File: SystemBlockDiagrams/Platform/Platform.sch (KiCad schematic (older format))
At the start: 21 parts

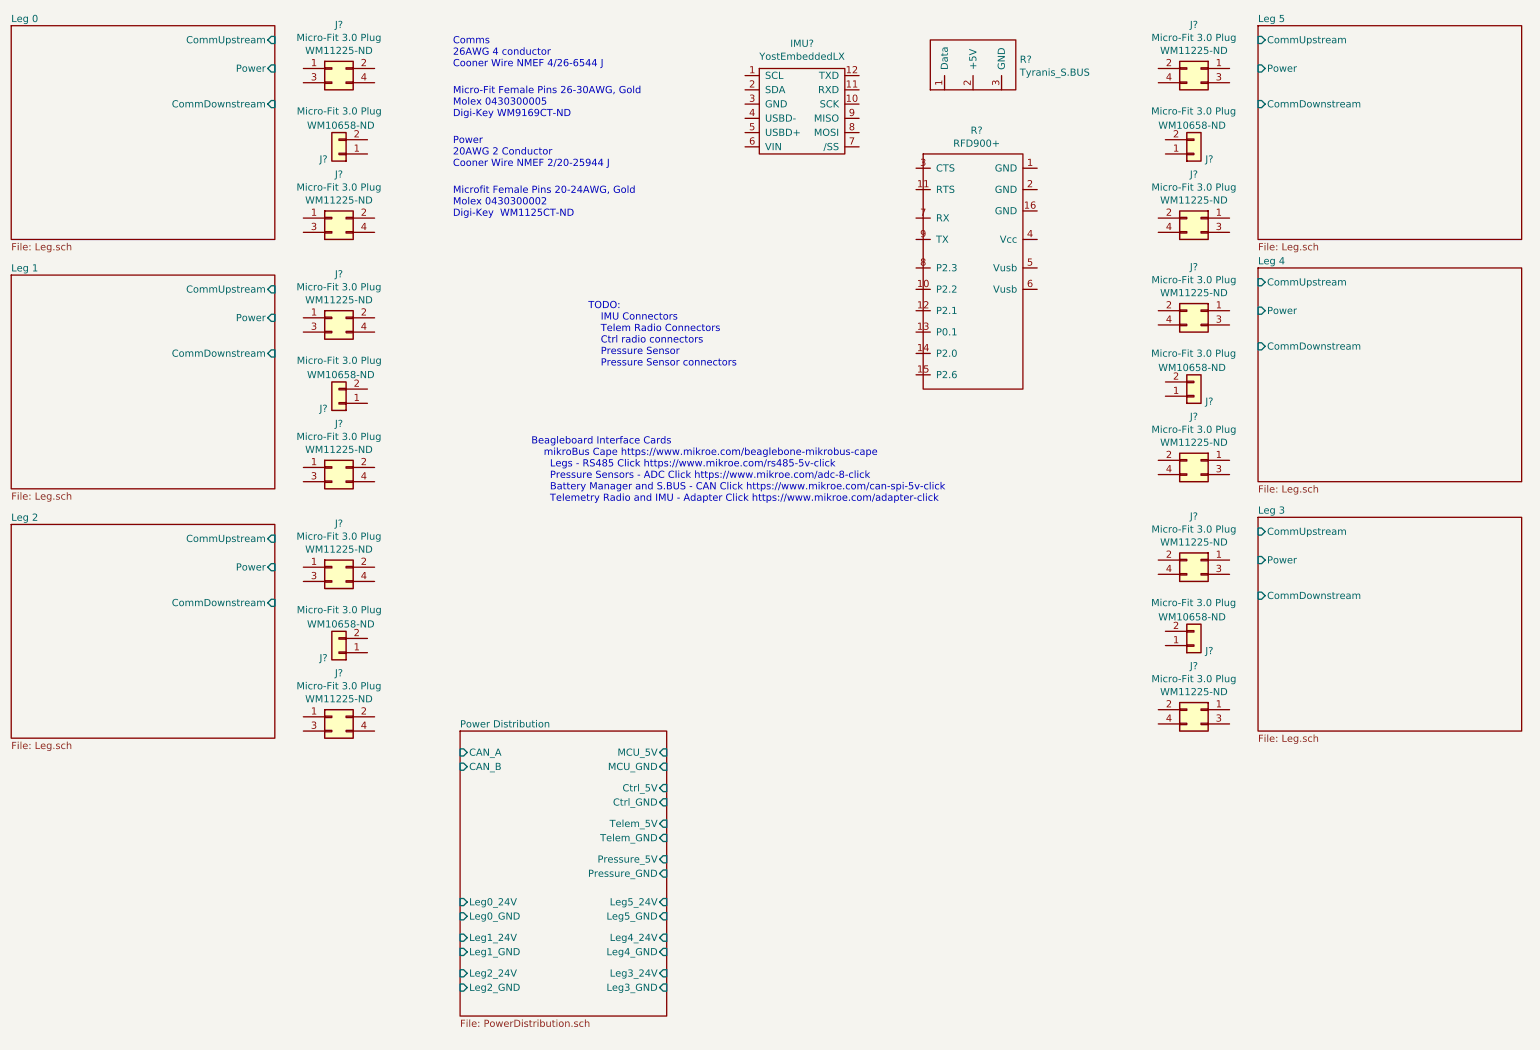
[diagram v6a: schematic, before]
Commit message: Adjust electronics hierarchy to match mechanicals.
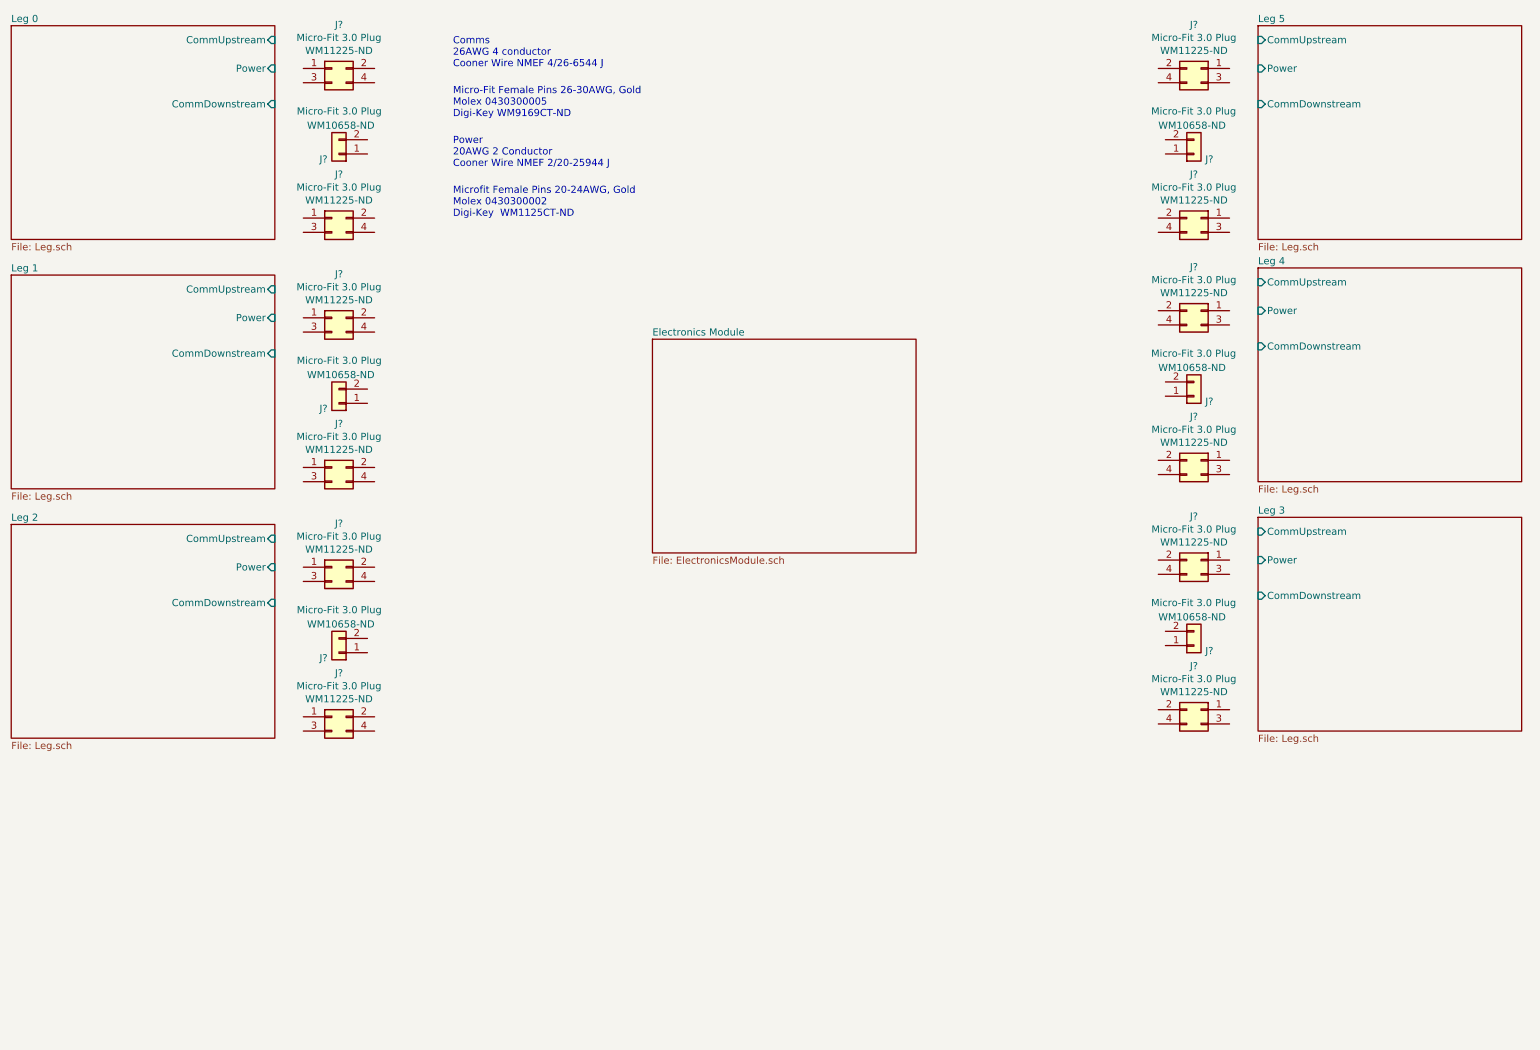
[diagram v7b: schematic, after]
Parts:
- removed IMU?: YostEmbeddedLX, symbol Stomp:YostEmbeddedLX
- removed R?: Tyranis_S.BUS, symbol Stomp:Tyranis_S.BUS
- removed R?: RFD900+, symbol Stomp:RFD900+
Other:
- note removed: "Beagleboard Interface Cards\n mikroBus Cape https://www.mikroe.com/beaglebone-mikrobus-cape\n Legs - RS485 Click https://www.mikroe.com/rs485-5v-click\n Pressure Sensors - ADC Click https://www.mikroe.com/adc-8-click\n Battery Manager and S.BUS - CAN Click https://www.mikroe.com/can-spi-5v-click\n Telemetry Radio and IMU - Adapter Click https://www.mikroe.com/adapter-click"
- note removed: "TODO:\n IMU Connectors\n Telem Radio Connectors\n Ctrl radio connectors\n Pressure Sensor\n Pressure Sensor connectors\n"
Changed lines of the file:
@@
 $Descr A4 11693 8268
 encoding utf-8
-Sheet 1 15
+Sheet 1 16
 Title ""
 Date ""
@@
 F4 "CommUpstream" I L 9300 700 50
 $EndSheet
-$Comp
-L Stomp:Tyranis_S.BUS R?
-U 1 1 5E2861EE
-P 7300 1050
-F 0 "R?" V 7513 722 50  0000 R CNN
-F 1 "Tyranis_S.BUS" V 7422 722 50  0000 R CNN
-F 2 "" H 7300 1050 50  0001 C CNN
-F 3 "" H 7300 1050 50  0001 C CNN
-	1    7300 1050
-	0    -1   -1   0
-$EndComp
-$Comp
-L Stomp:RFD900+ R?
-U 1 1 5E28A674
-P 7300 2300
-F 0 "R?" H 7325 3265 50  0000 C CNN
-F 1 "RFD900+" H 7325 3174 50  0000 C CNN
-F 2 "" H 6900 3350 50  0001 C CNN
-F 3 "" H 6900 3350 50  0001 C CNN
-	1    7300 2300
-	1    0    0    -1
-$EndComp
-Text Notes 4600 3000 0    50   ~ 0
-TODO:\n    IMU Connectors\n    Telem Radio Connectors\n    Ctrl radio connectors\n    Pressure Sensor\n    Pressure Sensor connectors\n
-$Sheet
-S 3700 5550 1450 2000
-U 5E269D05
-F0 "Power Distribution" 50
-F1 "PowerDistribution.sch" 50
-F2 "MCU_5V" I R 5150 5700 50
-F3 "MCU_GND" I R 5150 5800 50
-F4 "Ctrl_5V" I R 5150 5950 50
-F5 "Ctrl_GND" I R 5150 6050 50
-F6 "Telem_5V" I R 5150 6200 50
-F7 "Telem_GND" I R 5150 6300 50
-F8 "Pressure_5V" I R 5150 6450 50
-F9 "Pressure_GND" I R 5150 6550 50
-F10 "Leg0_24V" I L 3700 6750 50
-F11 "Leg0_GND" I L 3700 6850 50
-F12 "Leg1_24V" I L 3700 7000 50
-F13 "Leg1_GND" I L 3700 7100 50
-F14 "Leg2_24V" I L 3700 7250 50
-F15 "Leg2_GND" I L 3700 7350 50
-F16 "Leg3_GND" I R 5150 7350 50
-F17 "Leg3_24V" I R 5150 7250 50
-F18 "Leg4_GND" I R 5150 7100 50
-F19 "Leg4_24V" I R 5150 7000 50
-F20 "Leg5_GND" I R 5150 6850 50
-F21 "Leg5_24V" I R 5150 6750 50
-F22 "CAN_A" I L 3700 5700 50
-F23 "CAN_B" I L 3700 5800 50
-$EndSheet
-$Comp
-L Stomp:YostEmbeddedLX IMU?
-U 1 1 5E27BFDD
-P 6100 1200
-F 0 "IMU?" H 6100 1675 50  0000 C CNN
-F 1 "YostEmbeddedLX" H 6100 1584 50  0000 C CNN
-F 2 "" H 5950 1550 50  0001 C CNN
-F 3 "https://yostlabs.com/wp/wp-content/uploads/pdf/3-Space-Sensor-Users-Manual-Embedded-LX.pdf" H 5950 1550 50  0001 C CNN
-F 4 "Yost Labs" H 6100 1200 50  0001 C CNN "Supplier"
-F 5 "TSS_LX" H 6100 1200 50  0001 C CNN "Supplier Part Number"
-	1    6100 1200
-	1    0    0    -1
-$EndComp
-Text Notes 4200 3950 0    50   ~ 0
-Beagleboard Interface Cards\n    mikroBus Cape https://www.mikroe.com/beaglebone-mikrobus-cape\n      Legs - RS485 Click https://www.mikroe.com/rs485-5v-click\n      Pressure Sensors - ADC Click https://www.mikroe.com/adc-8-click\n      Battery Manager and S.BUS - CAN Click https://www.mikroe.com/can-spi-5v-click\n      Telemetry Radio and IMU - Adapter Click https://www.mikroe.com/adapter-click
+$Sheet
+S 5050 2800 1850 1500
+U 5E35EB39
+F0 "Electronics Module" 50
+F1 "ElectronicsModule.sch" 50
+$EndSheet
 $EndSCHEMATC

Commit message: Update part numbers for BOM generation
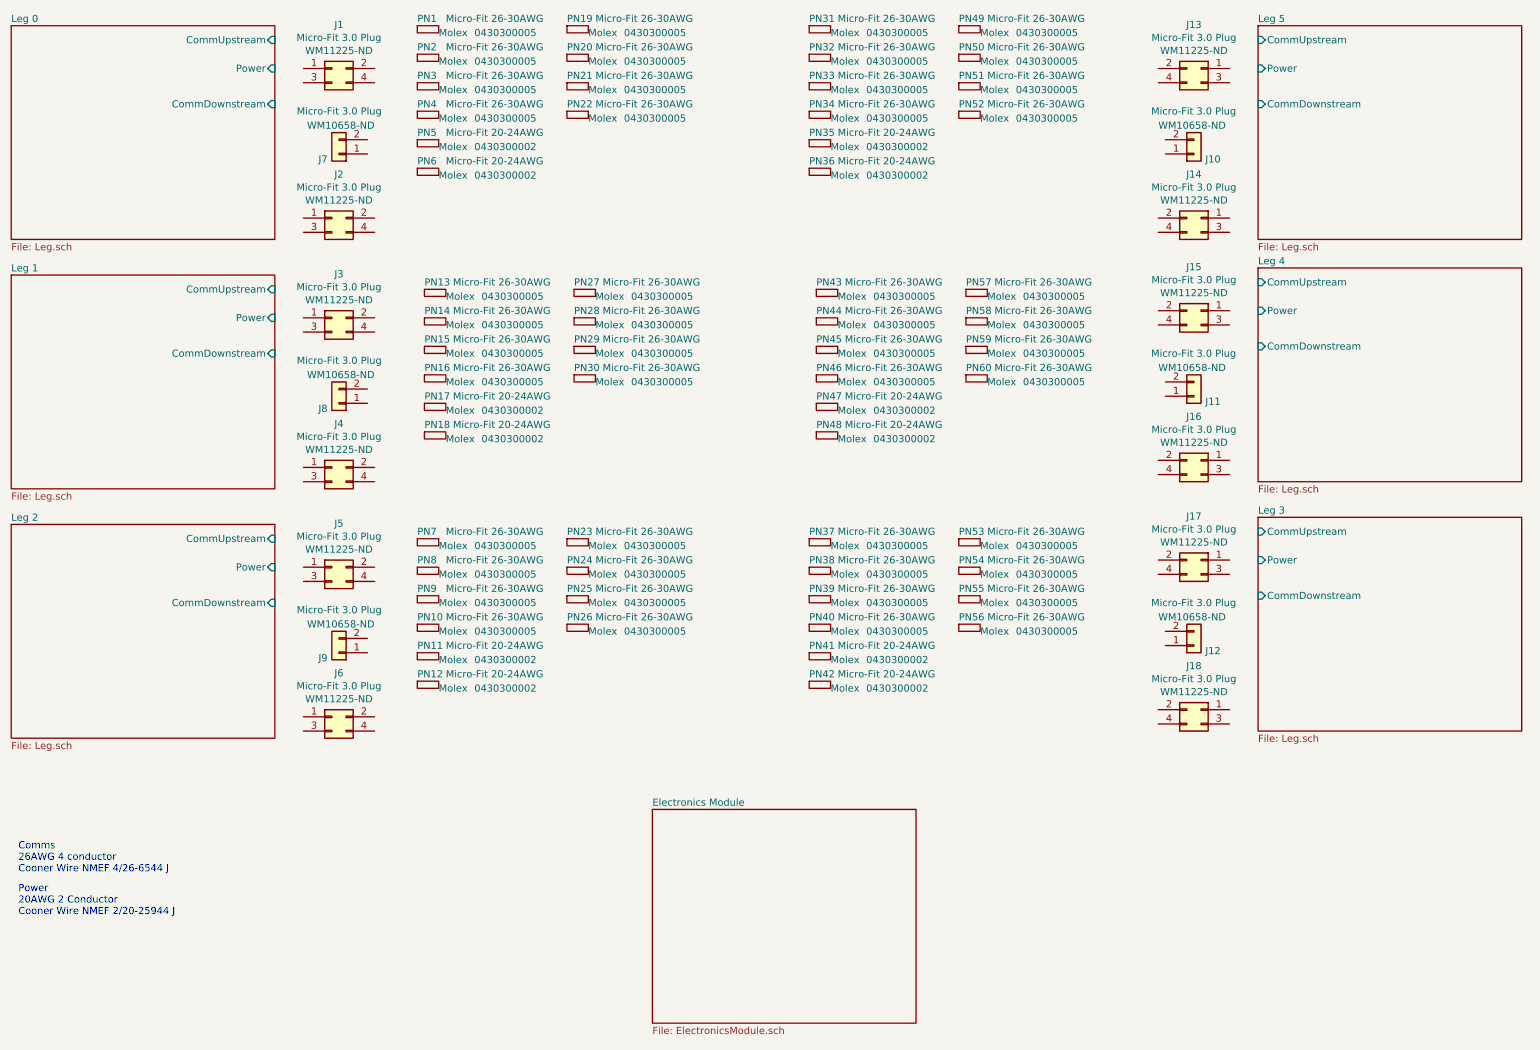
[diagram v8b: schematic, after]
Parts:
- added PN1, PN10, PN13, PN14, PN15, PN16, PN19, PN2, PN20, PN21, PN22, PN23, PN24, PN25, PN26, PN27, PN28, PN29, PN3, PN30, PN31, PN32, PN33, PN34, PN37, PN38, PN39, PN4, PN40, PN43, PN44, PN45, PN46, PN49, PN50, PN51, PN52, PN53, PN54, PN55, PN56, PN57, PN58, PN59, PN60, PN7, PN8, PN9: Micro-Fit 26-30AWG, symbol Stomp:PIN
- added PN11, PN12, PN17, PN18, PN35, PN36, PN41, PN42, PN47, PN48, PN5, PN6: Micro-Fit 20-24AWG, symbol Stomp:PIN
- J1, J13, J14, J15, J16, J17, J18, J2, J3, J4, J5, J6: renamed from J?; Manufacturer Part Number (none) -> 0430250408; Manufacturer part Number 0430250408 -> (none)
- J10, J11, J12, J7, J8, J9: renamed from J?; Manufacturer (none) -> Molex; Manufacturer Part Number (none) -> 0436450208; Manufacturer part Number 0436450208 -> (none); Supplier Part Number (none) -> WM10658-ND; Supplier part Number WM10658-ND -> (none); manufacturer Molex -> (none)
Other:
- note removed: "Micro-Fit Female Pins 26-30AWG, Gold\nMolex 0430300005\nDigi-Key WM9169CT-ND"
- note removed: "Microfit Female Pins 20-24AWG, Gold\nMolex 0430300002\nDigi-Key WM1125CT-ND"
